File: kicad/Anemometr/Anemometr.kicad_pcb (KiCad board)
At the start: 2 copper layers, 44.9 x 45.2 mm, 162 parts, among them J10 +Z3, J11 -Z3, J12 +Z4, J13 -Z4, J14 SWD, J15 SWC, J18 1 TxD+, J19 2 TxD-, J2 Conn_01x01_Female, J20 3 RxD+, J21 4-5, J23 6 RxD-, J24 7-8, J3 RST, J36 TMP117, J37 TMP117, J38 TMP117, J39 TMP117, J4 TxD, J5 RxD, J6 +Z1, J7 -Z1, J8 +Z2, J9 -Z2, Q1 5N10, U1 TS5A3166DBVR, U10 MCP1700-3002E, U2 LMV7239, U3 TS5A3166DBVR, U4 TS5A3166DBVR, U5 STM32F103C8Tx, U6 TS5A3166DBVR, U7 LM2734Y, U8 MCP1700-5002E, U9 MCP1700-3002E, Y1 8MHz, Y2 25MHz

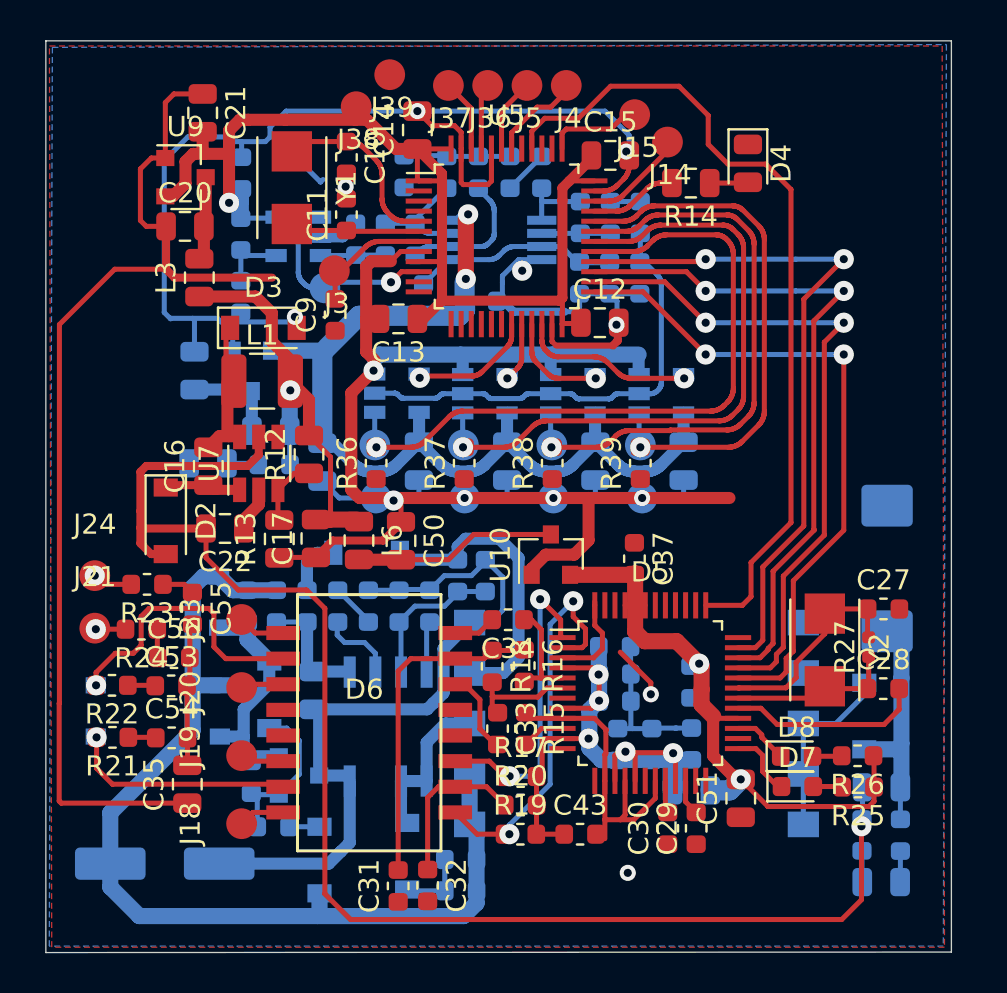
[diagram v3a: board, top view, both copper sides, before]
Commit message: изменено:      kicad/Anemometr/Anemometr-cache.lib 	изменено:      kicad/Anemometr/Anemometr-rescue.lib 	изменено:      kicad/Anemometr/Anemometr.kicad_pcb 	изменено:      kicad/Anemometr/Anemometr.kicad_pcb-bak 	изменено:      kicad/Anemometr/Anemometr.sch 	изменено:      kicad/Anemometr/Anemometr.sch-bak 	изменено:      stm32cubeide/Anemometer/.mxproject 	изменено:      stm32cubeide/Anemometer/.settings/language.settings.xml 	изменено:      stm32cubeide/Anemometer/Anemometer.ioc 	новый файл:    stm32cubeide/Anemometer/Core/Inc/dhcp.h 	новый файл:    stm32cubeide/Anemometer/Core/Inc/dns.h 	изменено:      stm32cubeide/Anemometer/Core/Inc/main.h 	новый файл:    stm32cubeide/Anemometer/Core/Inc/socket.h 	изменено:      stm32cubeide/Anemometer/Core/Inc/wizchip_conf.h 	изменено:      stm32cubeide/Anemometer/Debug/Anemometer.bin 	изменено:      stm32cubeide/Anemometer/Debug/Anemometer.elf 	изменено:      stm32cubeide/Anemometer/Debug/Anemometer.list 	изменено:      stm32cubeide/Anemometer/Debug/Anemometer.map 	изменено:      stm32cubeide/Anemometer/Debug/Core/Src/main.d 	изменено:      stm32cubeide/Anemometer/Debug/Core/Src/main.o 	изменено:      stm32cubeide/Anemometer/Debug/Core/Src/main.su 	изменено:      stm32cubeide/Anemometer/Debug/Core/Src/stm32f1xx_hal_msp.d 	изменено:      stm32cubeide/Anemometer/Debug/Core/Src/stm32f1xx_hal_msp.o 	изменено:      stm32cubeide/Anemometer/Debug/Core/Src/stm32f1xx_hal_msp.su 	изменено:      stm32cubeide/Anemometer/Debug/Core/Src/stm32f1xx_it.d 	изменено:      stm32cubeide/Anemometer/Debug/Core/Src/stm32f1xx_it.o 	изменено:      stm32cubeide/Anemometer/Debug/Core/Src/stm32f1xx_it.su 	изменено:      stm32cubeide/Anemometer/Debug/Core/Src/subdir.mk 	изменено:      stm32cubeide/Anemometer/Debug/Core/Src/system_stm32f1xx.d 	изменено:      stm32cubeide/Anemometer/Debug/Core/Src/system_stm32f1xx.o 	изменено:      stm32cubeide/Anemometer/Debug/Drivers/STM32F1xx_HAL_Driver/Src/stm32f1xx_hal.d 	изменено:      stm32cubeide/Anemometer/Debug/Dr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
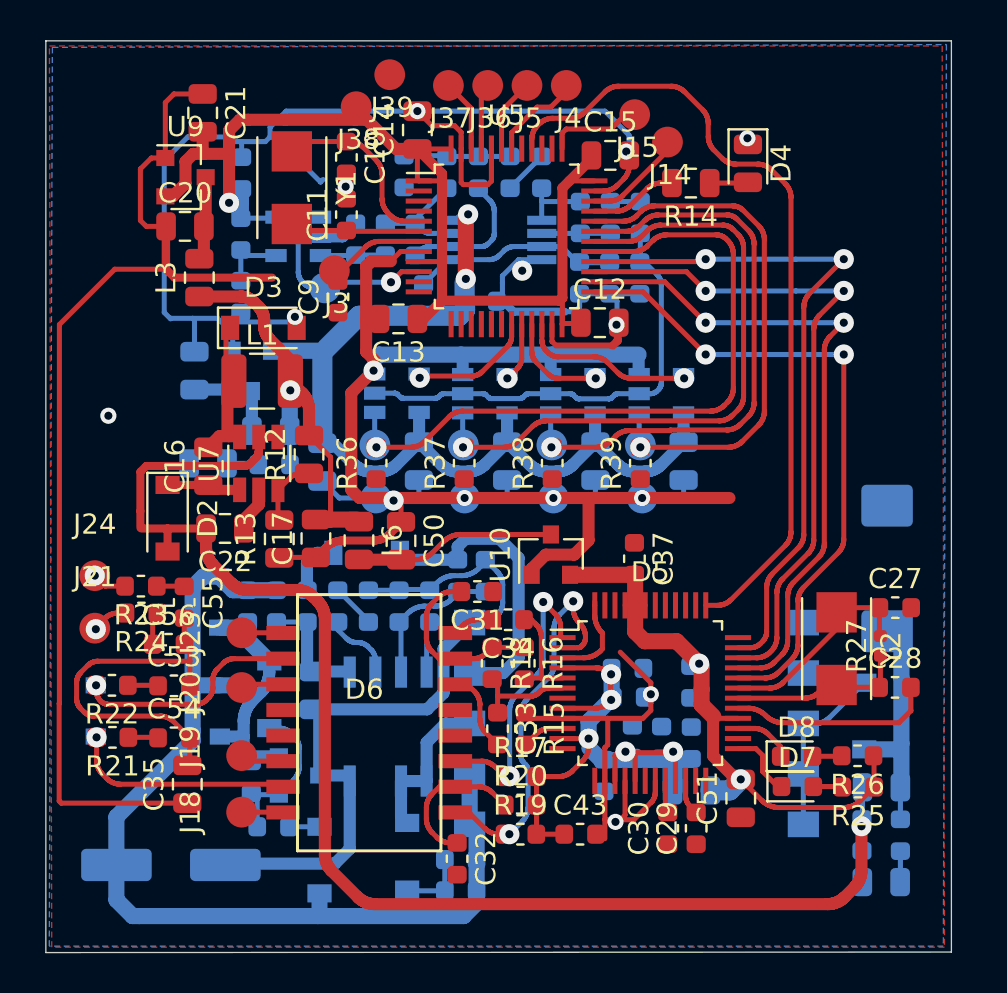
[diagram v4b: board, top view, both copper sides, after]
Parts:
- moved C31 15.1 mm to (40.3, 86.9), turned to 180 degrees
- moved C44 6.41 mm to (46.5, 96.0), turned to 270 degrees
- moved C32 1.97 mm to (39.3, 100.1)
- moved C9 0.90 mm to (33.4, 72.3)
- moved R24 0.80 mm to (23.6, 88.0)
- moved C40 0.74 mm to (47.9, 94.3)
- moved C42 0.72 mm to (47.8, 92.1)
- moved C56 0.71 mm to (25.0, 89.5)
- moved C41 0.68 mm to (47.7, 90.7)
- moved J23 0.66 mm to (28.6, 88.9)
- moved C27 0.59 mm to (61.0, 87.7)
- moved C28 0.59 mm to (61.0, 91.6)
- moved R27 0.59 mm to (60.2, 89.6)
- moved Y2 0.59 mm to (58.1, 89.7)
- moved J18 0.57 mm to (28.6, 97.8)
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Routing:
- net Net-(C35-Pad2): track 7.11 -> 18.5 mm
- net Net-(C31-Pad2): track 16.5 -> 9.11 mm
- net GND: track 265.4 -> 261.6 mm, vias 13 -> 15
- net Net-(C22-Pad2): track 71.7 -> 68.0 mm
- net Net-(D6-Pad10): track 14.1 -> 11.3 mm
- net Net-(D5-Pad1): track 15.2 -> 14.1 mm
- net Net-(D5-Pad37): track 41.0 -> 40.0 mm
- net +3.3VA: track 32.8 -> 33.6 mm
- net Net-(C9-Pad2): track 6.11 -> 5.33 mm

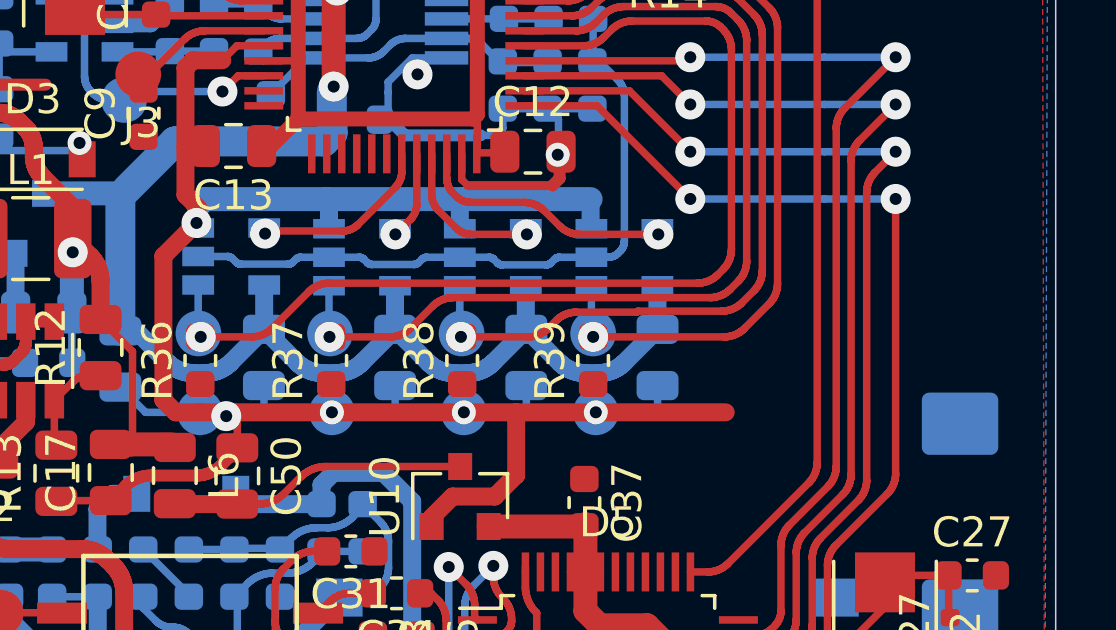
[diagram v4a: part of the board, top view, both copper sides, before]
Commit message: изменено:      kicad/Anemometr/Anemometr.kicad_pcb 	изменено:      kicad/Anemometr/Anemometr.kicad_pcb-bak
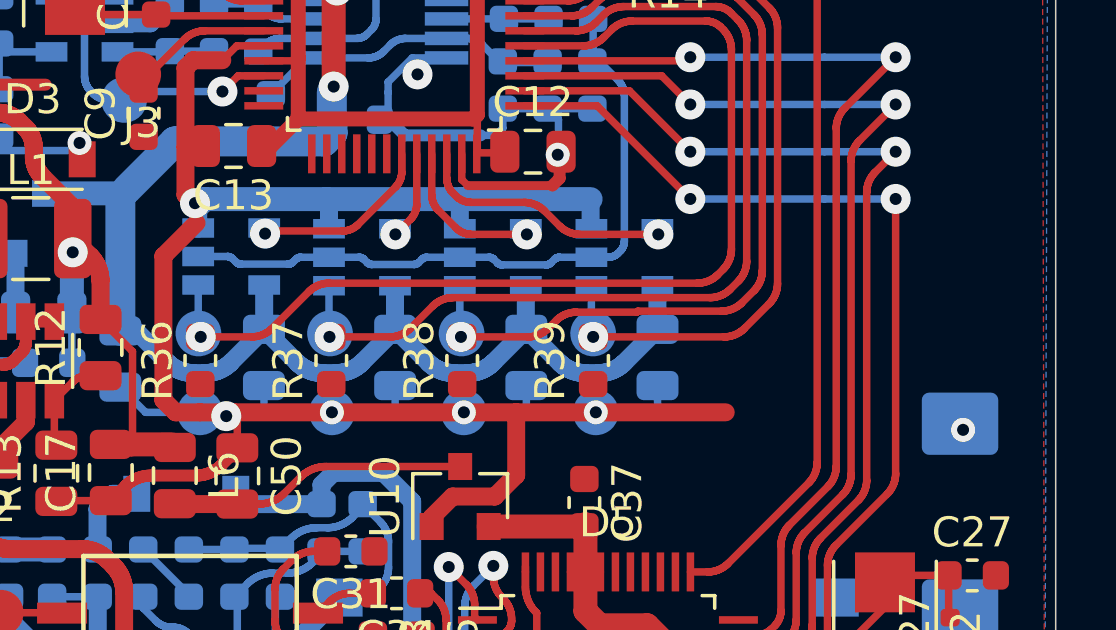
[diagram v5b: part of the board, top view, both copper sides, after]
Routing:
- net GND: vias 15 -> 16
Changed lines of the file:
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@@
     (thickness 1.6)
     (drawings 6)
-    (tracks 4331)
+    (tracks 4332)
     (zones 0)
     (modules 162)
@@
   (gr_line (start 63.754 59.6011) (end 63.754 104.7623) (layer Edge.Cuts) (width 0.05))
   (gr_line (start 18.8722 59.6011) (end 63.754 59.6011) (layer Edge.Cuts) (width 0.05))
+  (via (at 60.6679 82.8421) (size 0.8) (drill 0.4) (layers F.Cu B.Cu) (net 1))
   (via (at 31.2166 73.279) (size 0.8) (drill 0.4) (layers F.Cu B.Cu) (net 1))
   (segment (start 41.5013 72.4662) (end 41.5013 71.5922) (width 0.25) (layer B.Cu) (net 1))
@@
   (segment (start 41.5013 71.5922) (end 41.5013 71.2493) (width 0.25) (layer B.Cu) (net 1))
   (via (at 42.4815 70.993) (size 1) (drill 0.4) (layers F.Cu B.Cu) (net 1))
-  (via (at 35.1155 75.946) (size 1) (drill 0.4) (layers F.Cu B.Cu) (net 1))
+  (via (at 35.0647 75.2856) (size 1) (drill 0.4) (layers F.Cu B.Cu) (net 1))
   (segment (start 35.1178 75.4865) (end 35.1712 75.4331) (width 0.25) (layer F.Cu) (net 1))
   (segment (start 33.7312 67.3861) (end 33.7693 67.4242) (width 0.25) (layer F.Cu) (net 1))

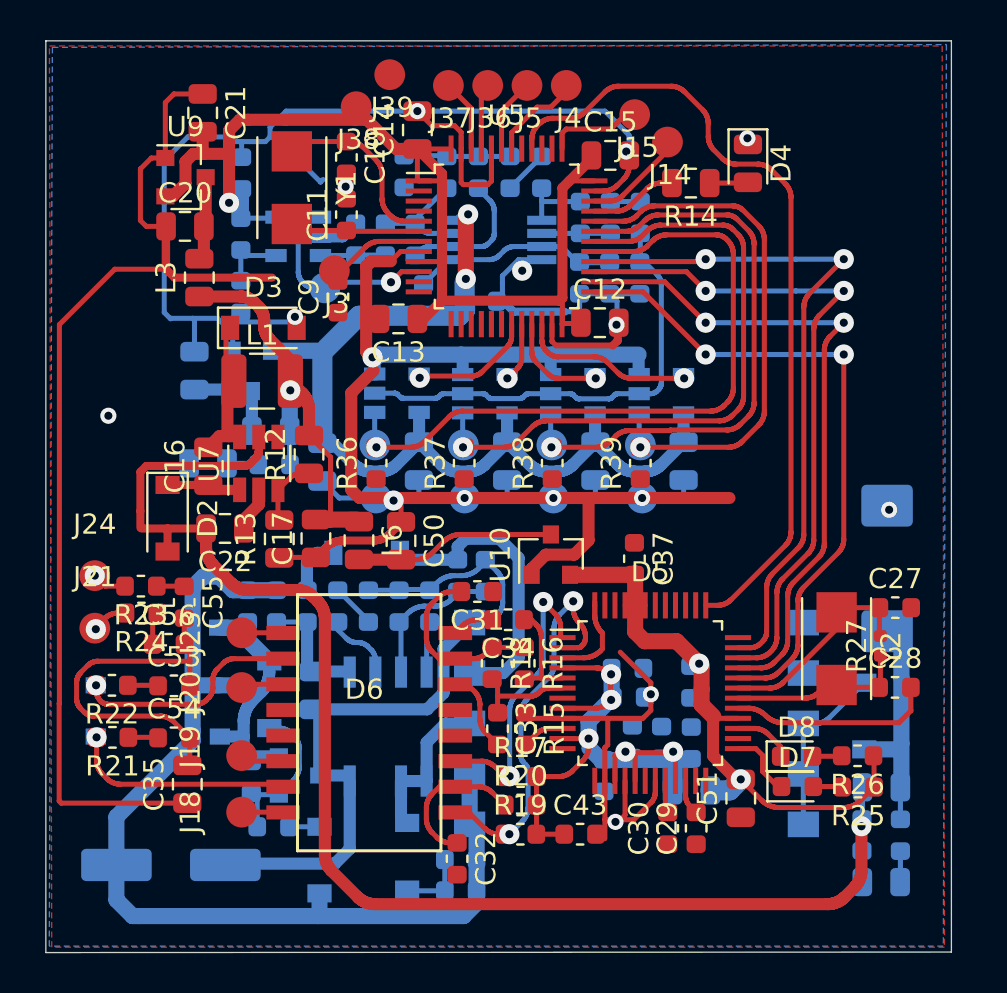
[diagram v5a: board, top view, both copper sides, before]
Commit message: изменено:      kicad/Anemometr/Anemometr.kicad_pcb 	изменено:      kicad/Anemometr/Anemometr.kicad_pcb-bak 	изменено:      kicad/Anemometr/Anemometr.sch 	изменено:      kicad/Anemometr/Anemometr.sch-bak
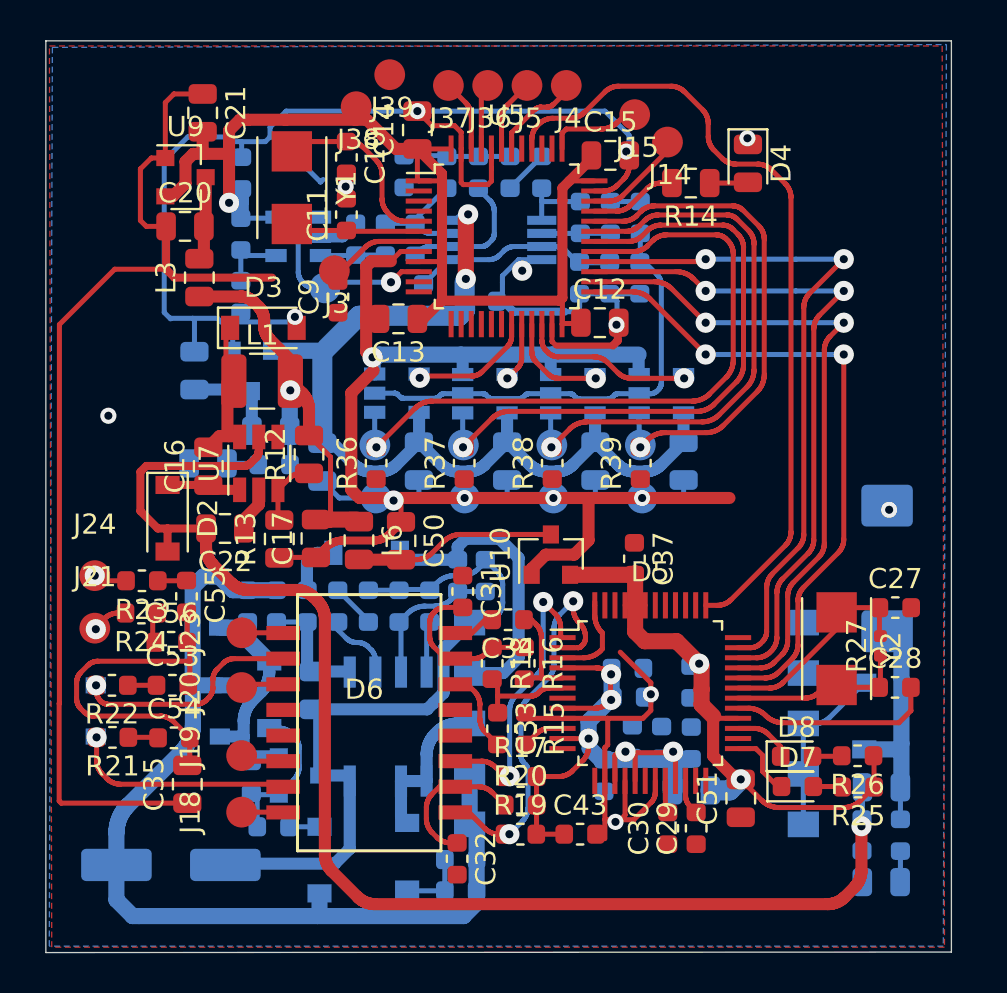
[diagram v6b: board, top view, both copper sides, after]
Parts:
- moved C31 0.72 mm to (39.5, 86.9), turned to 270 degrees
- moved C55 0.31 mm to (25.8, 87.1)
- moved R23 0.27 mm to (23.6, 86.4)
- moved C56 0.16 mm to (25.1, 89.4)
- moved C53 0.08 mm to (25.1, 91.5)
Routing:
- net Net-(J12-Pad1): track 26.7 -> 25.7 mm
- net Net-(C31-Pad2): track 9.11 -> 8.23 mm
- net Net-(J8-Pad1): track 32.3 -> 31.5 mm
- net Net-(J10-Pad1): track 29.4 -> 28.6 mm
- net Net-(J6-Pad1): track 35.0 -> 34.3 mm

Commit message: изменено:      FreeCAD/base-4.FCStd 	изменено:      FreeCAD/base-4.stl 	изменено:      FreeCAD/cover-4.fcstd 	изменено:      FreeCAD/cover-4.stl 	изменено:      FreeCAD/holder-3.fcstd 	изменено:      kicad/Anemometr/Anemometr.kicad_pcb 	изменено:      kicad/Anemometr/Anemometr.kicad_pcb-bak 	изменено:      kicad/Anemometr/Anemometr.sch 	изменено:      kicad/Anemometr/Anemometr.sch-bak
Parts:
- removed R35: 2k, Resistor_SMD:R_0603_1608Metric
- J10, J11, J12, J13, J6, J7, J8, J9: moved to F.Cu
- moved C56 6.06 mm to (21.3, 94.1), turned to 270 degrees
- moved R21 4.94 mm to (25.9, 97.4), turned to 90 degrees
- moved C35 4.68 mm to (21.3, 97.3)
- moved R22 4.02 mm to (26.1, 92.0), turned to 90 degrees
- moved R24 3.98 mm to (21.3, 91.2), turned to 90 degrees
- moved C54 3.39 mm to (24.2, 97.4), turned to 90 degrees
- moved J9 1.99 mm to (37.2, 81.8)
- moved J7 1.97 mm to (41.6, 81.8)
- moved J13 1.95 mm to (45.9, 81.8)
- moved J11 1.93 mm to (50.3, 81.8)
- moved C55 1.89 mm to (24.2, 88.0), turned to 180 degrees
- moved C53 1.86 mm to (23.7, 92.7), turned to 180 degrees
- moved C23 1.30 mm to (41.7, 81.7)
- moved C24 1.30 mm to (37.4, 81.7)
- moved C25 1.30 mm to (50.5, 81.7)
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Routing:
- net GND: track 261.6 -> 236.5 mm
- net Net-(C35-Pad2): track 18.7 -> 12.7 mm
- net Net-(C49-Pad1): track 11.6 -> 10.0 mm
- net Net-(D10-Pad2): track 1.65 -> 2.23 mm
- net Net-(D6-Pad10): track 11.3 -> 10.8 mm

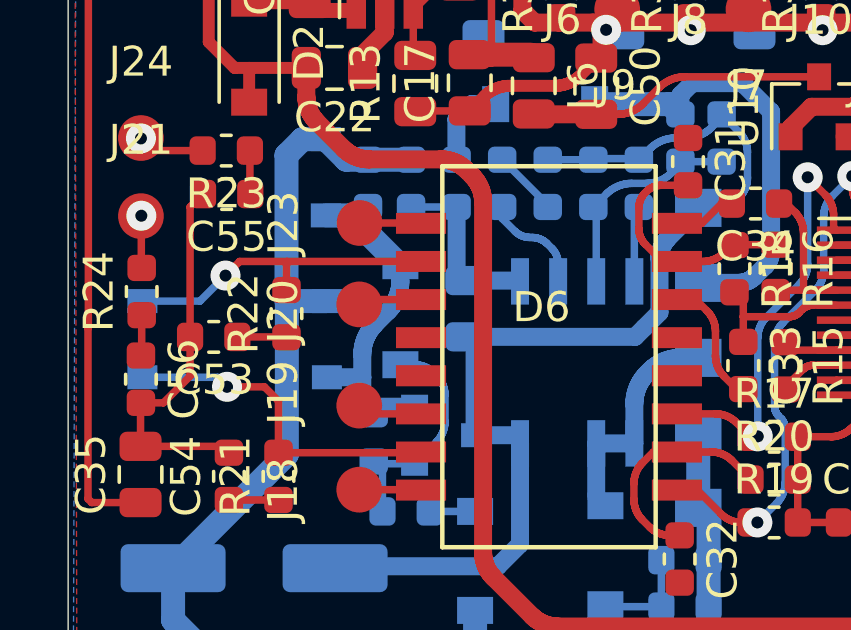
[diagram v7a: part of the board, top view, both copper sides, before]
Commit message: изменено:      kicad/Anemometr/Anemometr.kicad_pcb 	изменено:      kicad/Anemometr/Anemometr.kicad_pcb-bak 	изменено:      kicad/Anemometr/Anemometr.sch 	изменено:      kicad/Anemometr/Anemometr.sch-bak 	изменено:      kicad/Anemometr/fp-info-cache 	изменено:      stm32cubeide/Anemometer/.settings/language.settings.xml 	изменено:      stm32cubeide/Anemometer/Core/Inc/main.h 	изменено:      stm32cubeide/Anemometer/Core/Src/main.c 	изменено:      stm32cubeide/Anemometer/Core/Src/stm32f1xx_it.c 	изменено:      stm32cubeide/Anemometer/Release/Anemometer.bin 	изменено:      stm32cubeide/Anemometer/Release/Anemometer.elf 	изменено:      stm32cubeide/Anemometer/Release/Anemometer.list 	изменено:      stm32cubeide/Anemometer/Release/Anemometer.map 	изменено:      stm32cubeide/Anemometer/Release/Core/Src/main.d 	изменено:      stm32cubeide/Anemometer/Release/Core/Src/main.o 	изменено:      stm32cubeide/Anemometer/Release/Core/Src/main.su 	изменено:      stm32cubeide/Anemometer/Release/Core/Src/stm32f1xx_hal_msp.d 	изменено:      stm32cubeide/Anemometer/Release/Core/Src/stm32f1xx_it.d 	изменено:      stm32cubeide/Anemometer/Release/Core/Src/stm32f1xx_it.o 	изменено:      stm32cubeide/Anemometer/Release/Core/Src/stm32f1xx_it.su
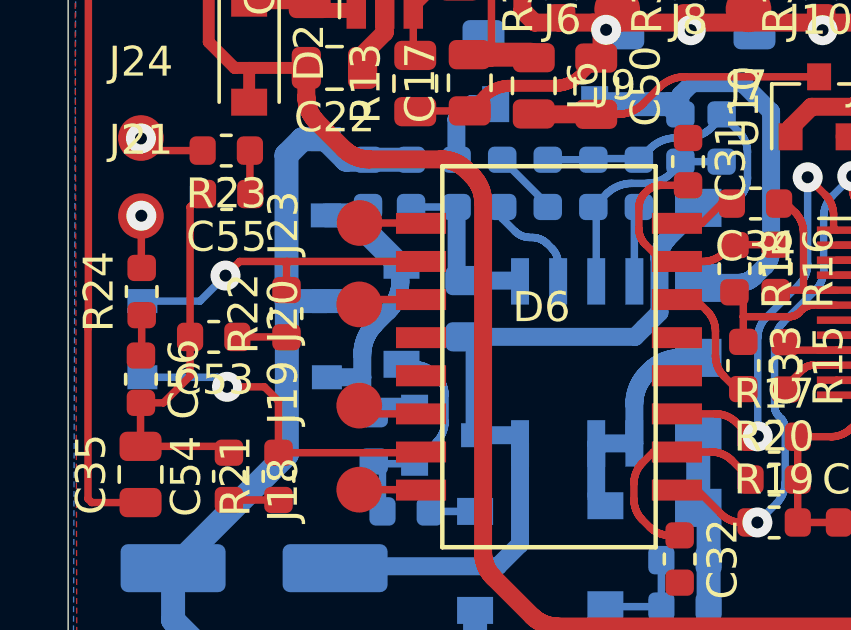
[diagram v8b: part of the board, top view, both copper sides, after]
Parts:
- turned D17 to 90 degrees
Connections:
- D17 pad 1: Net-(D10-Pad4) -> Net-(D17-Pad1)
- D17 pad 2: Net-(D17-Pad2) -> Net-(D10-Pad4)
- Q1 pad 1: Net-(D17-Pad2) -> Net-(D17-Pad1)
- R40 pad 1: Net-(D17-Pad2) -> Net-(D17-Pad1)
- R42 pad 1: Net-(D17-Pad2) -> Net-(D17-Pad1)
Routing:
- net Net-(D17-Pad2): track 7.89 -> 0.00 mm
- net Net-(D17-Pad1): track 0.00 -> 7.89 mm
